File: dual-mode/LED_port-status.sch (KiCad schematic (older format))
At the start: 19 parts, among them P1 CONN_9

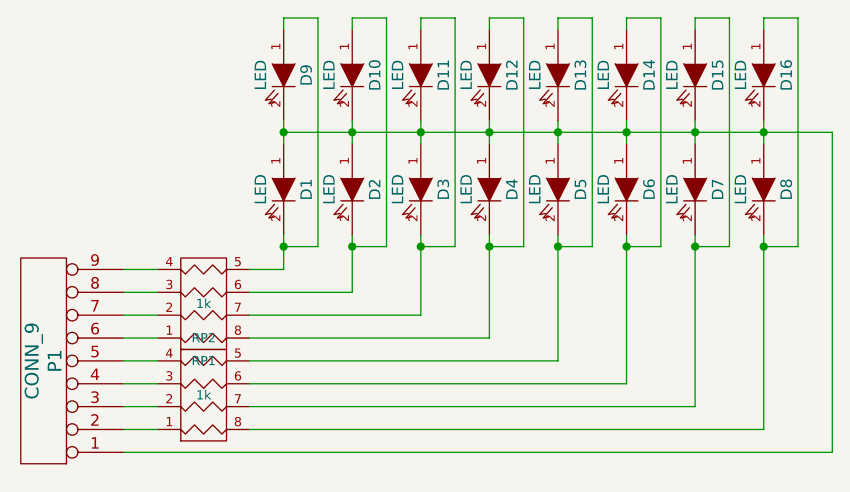
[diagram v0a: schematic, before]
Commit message: Updated 'dual-mode'.
* multi-footprints 0402-0603-0805
* silkscreen tweaks
* mask tweaks
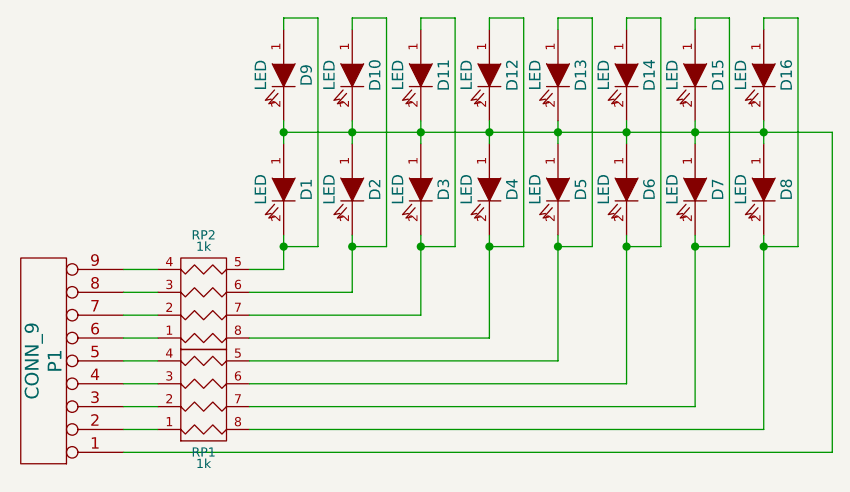
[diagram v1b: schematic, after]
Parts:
- D1, D10, D11, D12, D13, D14, D15, D16, D2, D3, D4, D5, D6, D7, D8, D9: footprint (none) -> my_parts:R_0805_0603_0402
- P1: footprint (none) -> SIL-Headers:SIL-9
- RP1, RP2: footprint (none) -> my_parts:MADW__1206x4_resistor_array
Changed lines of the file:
@@
-EESchema Schematic File Version 2  date Sun 17 Feb 2013 02:52:17 PM CET
-LIBS:power
-LIBS:device
-LIBS:transistors
-LIBS:conn
-LIBS:linear
-LIBS:regul
-LIBS:74xx
-LIBS:cmos4000
-LIBS:adc-dac
-LIBS:memory
-LIBS:xilinx
-LIBS:special
-LIBS:microcontrollers
-LIBS:dsp
-LIBS:microchip
-LIBS:analog_switches
-LIBS:motorola
-LIBS:texas
-LIBS:intel
-LIBS:audio
-LIBS:interface
-LIBS:digital-audio
-LIBS:philips
-LIBS:display
-LIBS:cypress
-LIBS:siliconi
-LIBS:opto
-LIBS:atmel
-LIBS:contrib
-LIBS:valves
+EESchema Schematic File Version 2
 LIBS:my_parts
 LIBS:LED_port-status-cache
-EELAYER 27 0
+EELAYER 25 0
 EELAYER END
 $Descr User 8268 5866
@@
 Sheet 1 1
 Title "LED_port-status"
-Date "17 feb 2013"
-Rev "0.2"
-Comp "2012 - blog.spitzenpfeil.org"
+Date "Tue 09 Jun 2015"
+Rev "0.21"
+Comp "2015 - blog.spitzenpfeil.org"
 Comment1 ""
 Comment2 ""
@@
 F 0 "P1" V 2150 3100 60  0000 C CNN
 F 1 "CONN_9" V 2250 3100 60  0000 C CNN
-F 2 "" H 2200 3100 60  0001 C CNN
+F 2 "SIL-Headers:SIL-9" H 2200 3100 60  0001 C CNN
 F 3 "" H 2200 3100 60  0001 C CNN
 	1    2200 3100
@@
 F 0 "D1" H 3250 2450 50  0000 C CNN
 F 1 "LED" H 3250 2250 50  0000 C CNN
-F 2 "" H 3250 2350 60  0001 C CNN
+F 2 "my_parts:R_0805_0603_0402" H 3250 2350 60  0001 C CNN
 F 3 "" H 3250 2350 60  0001 C CNN
 	1    3250 2350
@@
 F 0 "D3" H 3850 2450 50  0000 C CNN
 F 1 "LED" H 3850 2250 50  0000 C CNN
-F 2 "" H 3850 2350 60  0001 C CNN
+F 2 "my_parts:R_0805_0603_0402" H 3850 2350 60  0001 C CNN
 F 3 "" H 3850 2350 60  0001 C CNN
 	1    3850 2350
@@
 F 0 "D4" H 4150 2450 50  0000 C CNN
 F 1 "LED" H 4150 2250 50  0000 C CNN
-F 2 "" H 4150 2350 60  0001 C CNN
+F 2 "my_parts:R_0805_0603_0402" H 4150 2350 60  0001 C CNN
 F 3 "" H 4150 2350 60  0001 C CNN
 	1    4150 2350
@@
 F 0 "D5" H 4450 2450 50  0000 C CNN
 F 1 "LED" H 4450 2250 50  0000 C CNN
-F 2 "" H 4450 2350 60  0001 C CNN
+F 2 "my_parts:R_0805_0603_0402" H 4450 2350 60  0001 C CNN
 F 3 "" H 4450 2350 60  0001 C CNN
 	1    4450 2350
@@
 F 0 "D6" H 4750 2450 50  0000 C CNN
 F 1 "LED" H 4750 2250 50  0000 C CNN
-F 2 "" H 4750 2350 60  0001 C CNN
+F 2 "my_parts:R_0805_0603_0402" H 4750 2350 60  0001 C CNN
 F 3 "" H 4750 2350 60  0001 C CNN
 	1    4750 2350
@@
 F 0 "D7" H 5050 2450 50  0000 C CNN
 F 1 "LED" H 5050 2250 50  0000 C CNN
-F 2 "" H 5050 2350 60  0001 C CNN
+F 2 "my_parts:R_0805_0603_0402" H 5050 2350 60  0001 C CNN
 F 3 "" H 5050 2350 60  0001 C CNN
 	1    5050 2350
@@
 F 0 "D2" H 3550 2450 50  0000 C CNN
 F 1 "LED" H 3550 2250 50  0000 C CNN
-F 2 "" H 3550 2350 60  0001 C CNN
+F 2 "my_parts:R_0805_0603_0402" H 3550 2350 60  0001 C CNN
 F 3 "" H 3550 2350 60  0001 C CNN
 	1    3550 2350
@@
 F 0 "D8" H 5350 2450 50  0000 C CNN
 F 1 "LED" H 5350 2250 50  0000 C CNN
-F 2 "" H 5350 2350 60  0001 C CNN
+F 2 "my_parts:R_0805_0603_0402" H 5350 2350 60  0001 C CNN
 F 3 "" H 5350 2350 60  0001 C CNN
 	1    5350 2350
@@
 F 0 "D9" H 3250 1950 50  0000 C CNN
 F 1 "LED" H 3250 1750 50  0000 C CNN
-F 2 "" H 3250 1850 60  0001 C CNN
+F 2 "my_parts:R_0805_0603_0402" H 3250 1850 60  0001 C CNN
 F 3 "" H 3250 1850 60  0001 C CNN
 	1    3250 1850
@@
 F 0 "D11" H 3850 1950 50  0000 C CNN
 F 1 "LED" H 3850 1750 50  0000 C CNN
-F 2 "" H 3850 1850 60  0001 C CNN
+F 2 "my_parts:R_0805_0603_0402" H 3850 1850 60  0001 C CNN
 F 3 "" H 3850 1850 60  0001 C CNN
 	1    3850 1850
@@
 F 0 "D12" H 4150 1950 50  0000 C CNN
 F 1 "LED" H 4150 1750 50  0000 C CNN
-F 2 "" H 4150 1850 60  0001 C CNN
+F 2 "my_parts:R_0805_0603_0402" H 4150 1850 60  0001 C CNN
 F 3 "" H 4150 1850 60  0001 C CNN
 	1    4150 1850
@@
 F 0 "D13" H 4450 1950 50  0000 C CNN
 F 1 "LED" H 4450 1750 50  0000 C CNN
-F 2 "" H 4450 1850 60  0001 C CNN
+F 2 "my_parts:R_0805_0603_0402" H 4450 1850 60  0001 C CNN
 F 3 "" H 4450 1850 60  0001 C CNN
 	1    4450 1850
@@
 F 0 "D14" H 4750 1950 50  0000 C CNN
 F 1 "LED" H 4750 1750 50  0000 C CNN
-F 2 "" H 4750 1850 60  0001 C CNN
+F 2 "my_parts:R_0805_0603_0402" H 4750 1850 60  0001 C CNN
 F 3 "" H 4750 1850 60  0001 C CNN
 	1    4750 1850
@@
 F 0 "D15" H 5050 1950 50  0000 C CNN
 F 1 "LED" H 5050 1750 50  0000 C CNN
-F 2 "" H 5050 1850 60  0001 C CNN
+F 2 "my_parts:R_0805_0603_0402" H 5050 1850 60  0001 C CNN
 F 3 "" H 5050 1850 60  0001 C CNN
 	1    5050 1850
@@
 F 0 "D10" H 3550 1950 50  0000 C CNN
 F 1 "LED" H 3550 1750 50  0000 C CNN
-F 2 "" H 3550 1850 60  0001 C CNN
+F 2 "my_parts:R_0805_0603_0402" H 3550 1850 60  0001 C CNN
 F 3 "" H 3550 1850 60  0001 C CNN
 	1    3550 1850
@@
 F 0 "D16" H 5350 1950 50  0000 C CNN
 F 1 "LED" H 5350 1750 50  0000 C CNN
-F 2 "" H 5350 1850 60  0001 C CNN
+F 2 "my_parts:R_0805_0603_0402" H 5350 1850 60  0001 C CNN
 F 3 "" H 5350 1850 60  0001 C CNN
 	1    5350 1850
@@
 U 1 1 5120CCDC
 P 2900 2650
-F 0 "RP1" H 2900 3100 40  0000 C CNN
-F 1 "1k" H 2900 2850 40  0000 C CNN
-F 2 "" H 2900 2650 60  0000 C CNN
+F 0 "RP1" H 2900 3500 40  0000 C CNN
+F 1 "1k" H 2900 2600 40  0000 C CNN
+F 2 "my_parts:MADW__1206x4_resistor_array" H 2900 2650 60  0001 C CNN
 F 3 "" H 2900 2650 60  0000 C CNN
 	1    2900 2650
@@
 U 1 1 5120CD13
 P 2900 3050
-F 0 "RP2" H 2900 3000 40  0000 C CNN
-F 1 "1k" H 2900 3250 40  0000 C CNN
-F 2 "" H 2900 3050 60  0000 C CNN
+F 0 "RP2" H 2900 2550 40  0000 C CNN
+F 1 "1k" H 2900 3550 40  0000 C CNN
+F 2 "my_parts:MADW__1206x4_resistor_array" H 2900 3050 60  0001 C CNN
 F 3 "" H 2900 3050 60  0000 C CNN
 	1    2900 3050
